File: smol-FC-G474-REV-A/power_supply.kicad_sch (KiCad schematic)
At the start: 0 parts

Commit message: Updated Buck-5V doc, added Buck 5V/10V and LDO for 3v3 on schematic
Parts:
- added C30, C35, C40, C42: 1u, symbol Device:C_Small
- added C31, C34: 4.7u, symbol Device:C_Small
- added C32, C33: 47u, symbol Device:C_Small
- added C36, C37, C38: 22u, symbol Device:C_Small
- added C39, C41: 10u, symbol Device:C_Small
- added L1: 1.5u, symbol Device:L
- added L2: 2.2u, symbol Device:L
- added R22, R25: 7.68K, symbol Device:R_Small
- added R26: 90.9K, symbol Device:R_Small
- added R27, R28, R29: 10K, symbol Device:R_Small
- added U10, U9: LP5912-3.3DRV, Package_SON:WSON-6-1EP_2x2mm_P0.65mm_EP1x1.6mm, symbol Regulator_Linear:LP5912-3.3DRV
- added U7, U8: LMQ66430R5RXBR, RXB0014A-MFG, symbol LMQ66430:PLMQ66430R5RXBR
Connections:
- new net +10V: C36.1, C37.1, C38.1, L2.2, R26.1
- new net +3V3_CORE: C40.1, R28.1, U9.1 (OUT)
- new net +3V3_SENS: C42.1, R29.1, U10.1 (OUT)
- new net +5V_BEC: C32.1, C33.1, L1.2, U7.11 (VOUT_FB)
- new net +5V_SYS: C39.1, C41.1, U10.4 (EN), U10.6 (IN), U9.4 (EN), U9.6 (IN)
- new net +VBAT: C31.1, C34.1, U7.1 (EN), U7.3 (VIN), U8.1 (EN), U8.3 (VIN)
- new net Buck-10V_FB: R26.2, R27.1, U8.11 (VOUT_FB)
- new net Buck-10V_RT: R25.1, U8.13 (RT)
- new net Buck-10V_SW: L2.1, U8.7 (SW)
- new net Buck-10V_VCC_INT: C35.1, U8.10 (VCC)
- new net Buck-5V_RT: R22.1, U7.13 (RT)
- new net Buck-5V_SW: L1.1, U7.7 (SW)
- new net Buck-5V_VCC_INT: C30.1, U7.10 (VCC)
- new net GND: C30.2, C31.2, C32.2, C33.2, C34.2, C35.2, C36.2, C37.2, C38.2, C39.2, C40.2, C41.2, C42.2, R22.2, R25.2, R27.2, U10.5 (GND), U10.7 (EP), U7.15 (GND_DAP), U7.6 (PGND), U8.15 (GND_DAP), U8.6 (PGND), U9.5 (GND), U9.7 (EP)
- new net LDO-C_PG: R28.2, U9.3 (PG)
- new net LDO-S_PG: R29.2, U10.3 (PG)
- no-connect marks 0 -> 4

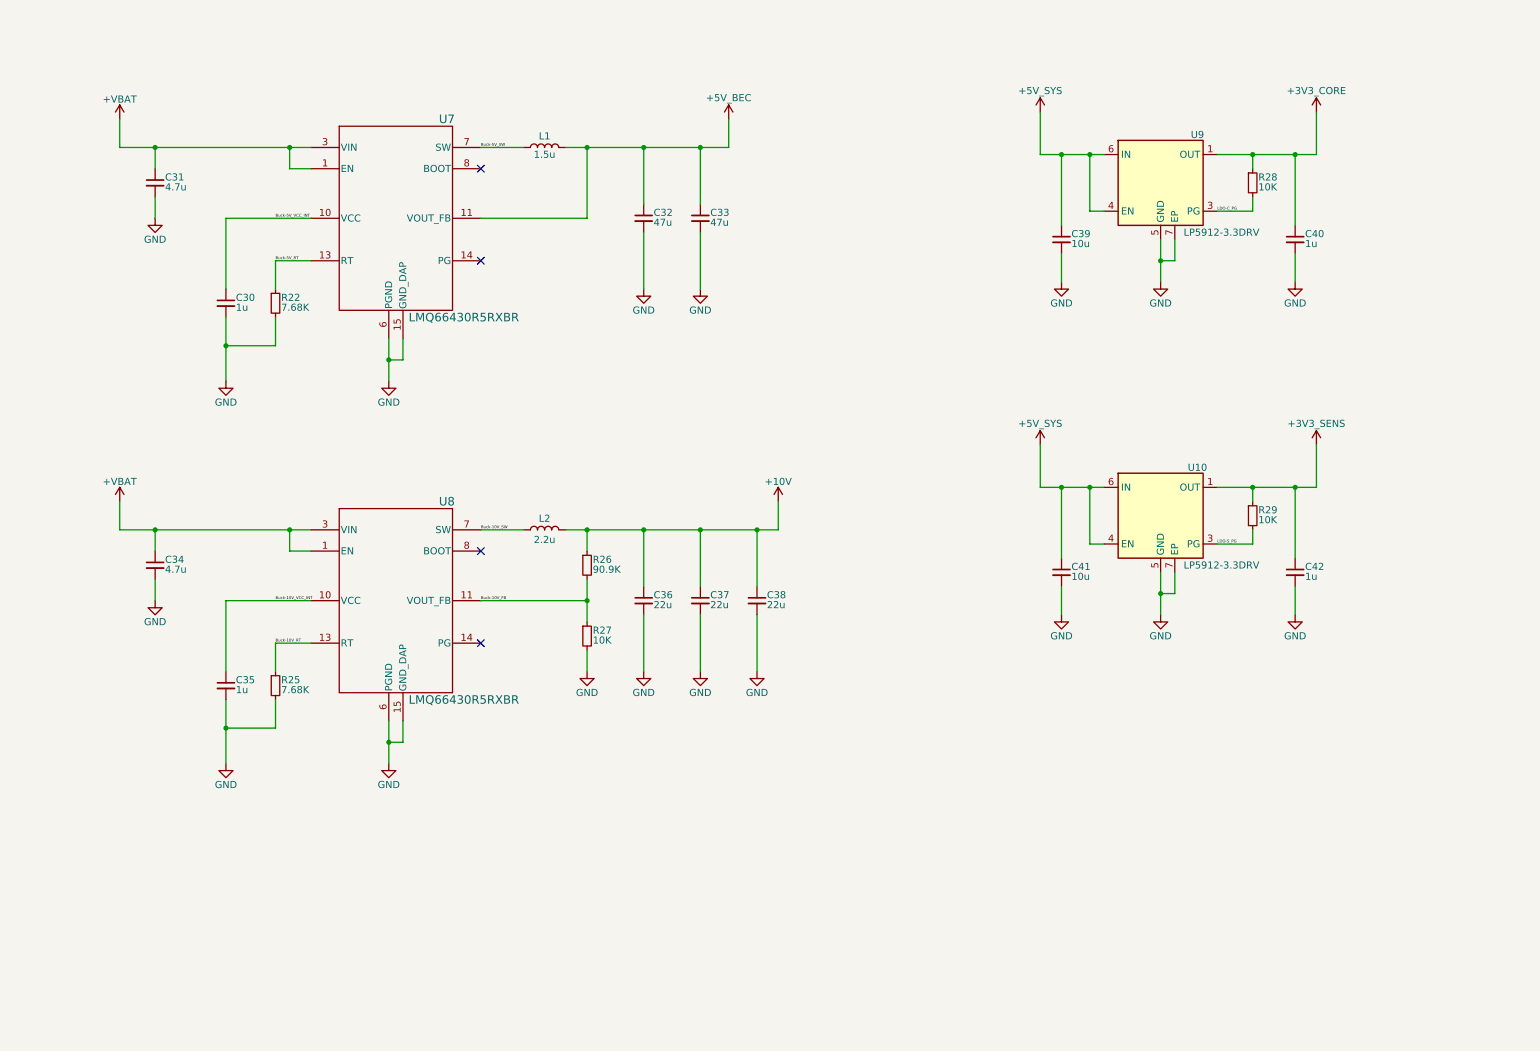
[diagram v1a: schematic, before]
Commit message: Changed 10V buck to 9V buck
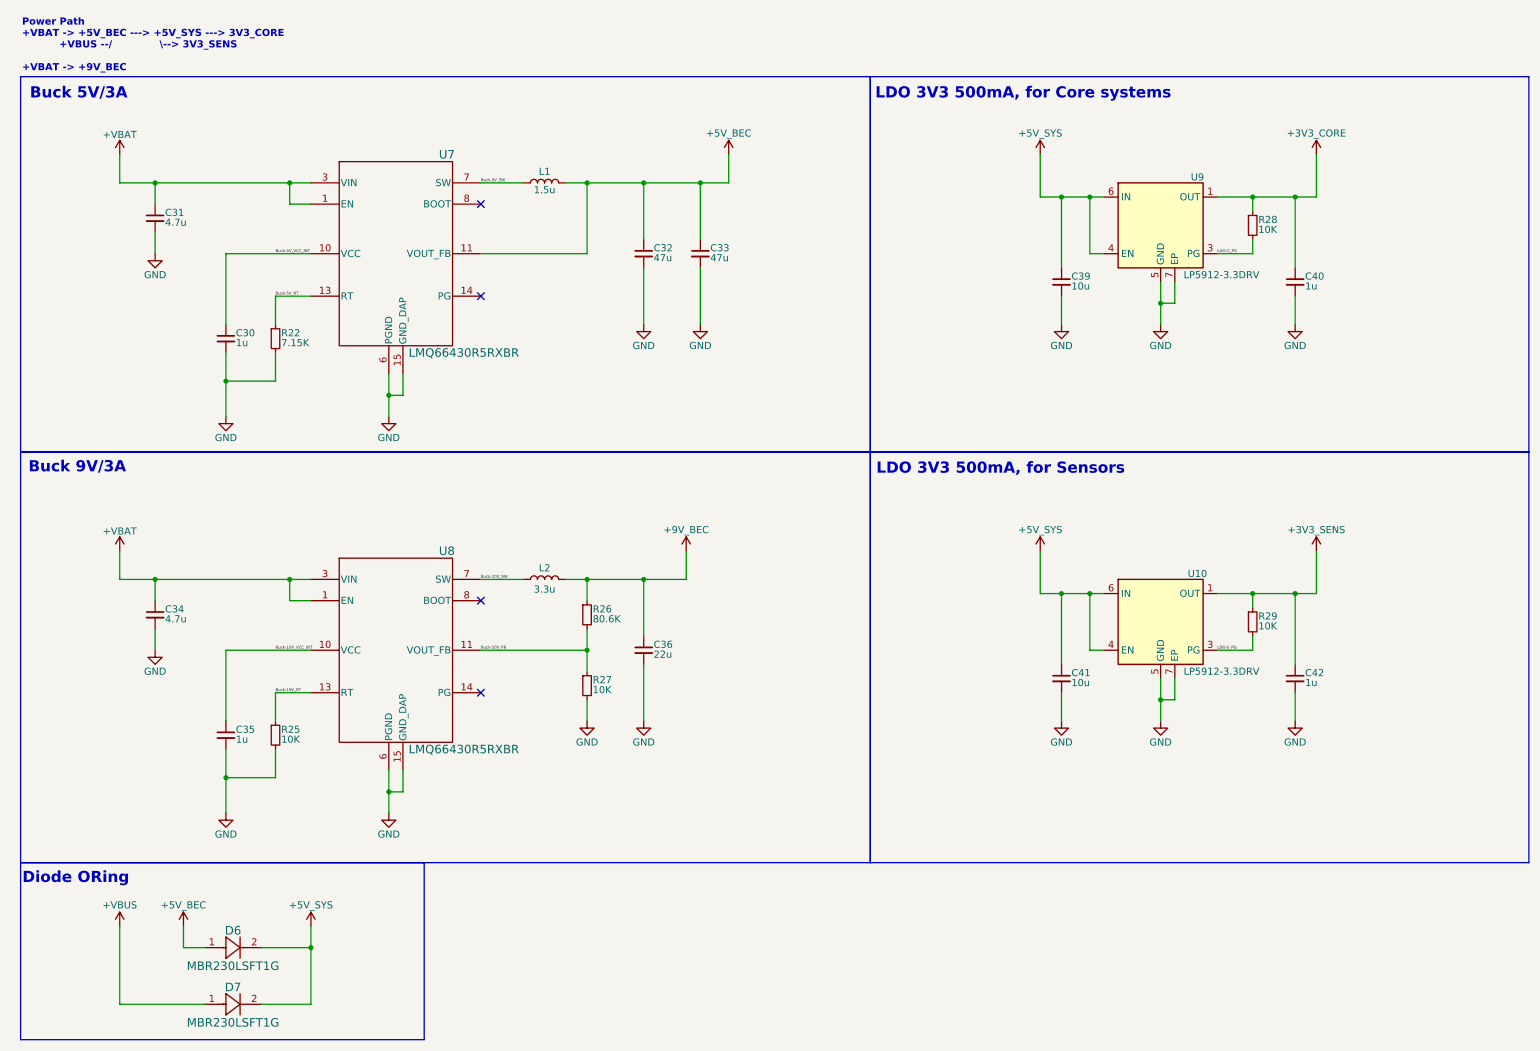
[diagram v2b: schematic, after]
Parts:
- removed C37, C38: 22u, symbol Device:C_Small
- added D6, D7: MBR230LSFT1G, symbol MBR230LSFT1G:MBR230LSFT1G
- L2: value 2.2u -> 3.3u
- R22: value 7.68K -> 7.15K
- R25: value 7.68K -> 10K
- R26: value 90.9K -> 80.6K
- U10, U9: footprint Package_SON:WSON-6-1EP_2x2mm_P0.65mm_EP1x1.6mm -> (none)
- U7, U8: footprint RXB0014A-MFG -> (none)
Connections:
- net +5V_BEC: now also D6.1
- net +5V_SYS: now also D6.2, D7.2
- net +10V renamed +9V_BEC
- new net +VBUS: D7.1
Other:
- note added: "Buck 5V/3A"
- note added: "Buck 9V/3A"
- note added: "Diode ORing"
- note added: "LDO 3V3 500mA, for Core systems"
- note added: "LDO 3V3 500mA, for Sensors"
- note added: "Power Path +VBAT -> +5V_BEC ---> +5V_SYS ---> 3V3_CORE +VBUS --/ \--> 3V3_SENS +VBAT -> +9V_BEC"
- moved on the sheet: C30, C31, C32, C33, C34, C35, C36, C39, C40, C41, C42, L1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

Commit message: Attached footprints and finalized schematic.
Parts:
- C30, C35: footprint (none) -> Capacitor_SMD:C_0603_1608Metric
- C31, C34: footprint (none) -> Capacitor_SMD:C_1206_3216Metric
- C32, C33, C36: footprint (none) -> Capacitor_SMD:C_0805_2012Metric
- C39, C40, C41, C42: footprint (none) -> Capacitor_SMD:C_0402_1005Metric
- D6, D7: footprint (none) -> MBR230LSFT1G:CR_0LSFT1G_ONS
- L1, L2: footprint (none) -> inductor-1.5u:AAPS0420M1R5F
- R22, R25, R26, R27, R28, R29: footprint (none) -> Resistor_SMD:R_0402_1005Metric
- U10, U9: footprint (none) -> Package_SON:WSON-6-1EP_2x2mm_P0.65mm_EP1x1.6mm
- U7, U8: footprint (none) -> LMQ66430:RXB0014A-MFG
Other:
- title: smol-FC-G474 -> smol-FC-G474-REV-A
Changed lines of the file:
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@@
 	(paper "A4")
 	(title_block
-		(title "smol-FC-G474")
-		(date "2026-05-31")
-		(rev "0.7.0")
+		(title "smol-FC-G474-REV-A")
+		(date "2026-06-05")
+		(rev "0.9.3")
 		(company "Daniel Plewa")
 		(comment 1 "License: CERN-OHL-W v2")
 		(comment 2 "GitHub: https://github.com/Def12345678/smol-FC-G474-REV-A")
-		(comment 3 "BEC 5A/2A, 10V/2A | Baro, OSD Chip and 16MB blackbox")
+		(comment 3 "BEC 5A/3A, 10V/3A | Baro, OSD Chip and 16MB blackbox")
 		(comment 4 "Open source flight controller on STM32G4, 20x20 3.5mm hole")
 	)
@@
 			)
 		)
-		(property "Footprint" ""
+		(property "Footprint" "inductor-1.5u:AAPS0420M1R5F"
 			(at 106.68 43.18 0)
 			(hide yes)
@@
 			)
 		)
-		(property "Footprint" ""
+		(property "Footprint" "Capacitor_SMD:C_0603_1608Metric"
 			(at 49.53 71.12 0)
 			(hide yes)
@@
 			)
 		)
-		(property "Footprint" ""
+		(property "Footprint" "Capacitor_SMD:C_0603_1608Metric"
 			(at 49.53 142.24 0)
 			(hide yes)
@@
 			)
 		)
-		(property "Footprint" ""
+		(property "Footprint" "Capacitor_SMD:C_1206_3216Metric"
 			(at 36.83 49.53 0)
 			(hide yes)
@@
 			)
 		)
-		(property "Footprint" ""
+		(property "Footprint" "Capacitor_SMD:C_0805_2012Metric"
 			(at 124.46 127 0)
 			(hide yes)
@@
 			)
 		)
-		(property "Footprint" ""
+		(property "Footprint" "Capacitor_SMD:C_0402_1005Metric"
 			(at 199.39 60.96 0)
 			(hide yes)
@@
 			)
 		)
-		(property "Footprint" ""
+		(property "Footprint" "Capacitor_SMD:C_0402_1005Metric"
 			(at 241.3 132.08 0)
 			(hide yes)
@@
 			)
 		)
-		(property "Footprint" ""
+		(property "Footprint" "Package_SON:WSON-6-1EP_2x2mm_P0.65mm_EP1x1.6mm"
 			(at 217.17 44.45 0)
 			(hide yes)
@@
 			)
 		)
-		(property "Footprint" ""
+		(property "Footprint" "Resistor_SMD:R_0402_1005Metric"
 			(at 114.3 133.35 0)
 			(hide yes)
@@
 			)
 		)
-		(property "Footprint" ""
+		(property "Footprint" "LMQ66430:RXB0014A-MFG"
 			(at 80.518 26.924 0)
 			(hide yes)
@@
 			)
 		)
-		(property "Footprint" ""
+		(property "Footprint" "MBR230LSFT1G:CR_0LSFT1G_ONS"
 			(at 55.88 190.5 0)
 			(hide yes)
@@
 			)
 		)
-		(property "Footprint" ""
+		(property "Footprint" "Capacitor_SMD:C_0402_1005Metric"
 			(at 199.39 132.08 0)
 			(hide yes)
@@
 			)
 		)
-		(property "Footprint" ""
+		(property "Footprint" "MBR230LSFT1G:CR_0LSFT1G_ONS"
 			(at 55.88 180.34 0)
 			(hide yes)
@@
 			)
 		)
-		(property "Footprint" ""
+		(property "Footprint" "Resistor_SMD:R_0402_1005Metric"
 			(at 58.42 71.12 0)
 			(hide yes)
@@
 			)
 		)
-		(property "Footprint" ""
+		(property "Footprint" "Package_SON:WSON-6-1EP_2x2mm_P0.65mm_EP1x1.6mm"
 			(at 217.17 115.57 0)
 			(hide yes)
@@
 			)
 		)
-		(property "Footprint" ""
+		(property "Footprint" "Capacitor_SMD:C_0805_2012Metric"
 			(at 134.62 55.88 0)
 			(hide yes)
@@
 			)
 		)
-		(property "Footprint" ""
+		(property "Footprint" "Capacitor_SMD:C_0805_2012Metric"
 			(at 124.46 55.88 0)
 			(hide yes)
@@
 			)
 		)
-		(property "Footprint" ""
+		(property "Footprint" "Capacitor_SMD:C_1206_3216Metric"
 			(at 36.83 120.65 0)
 			(hide yes)
@@
 			)
 		)
-		(property "Footprint" ""
+		(property "Footprint" "Capacitor_SMD:C_0402_1005Metric"
 			(at 241.3 60.96 0)
 			(hide yes)
@@
 			)
 		)
-		(property "Footprint" ""
+		(property "Footprint" "Resistor_SMD:R_0402_1005Metric"
 			(at 114.3 120.65 0)
 			(hide yes)
@@
 			)
 		)
-		(property "Footprint" ""
+		(property "Footprint" "Resistor_SMD:R_0402_1005Metric"
 			(at 233.68 50.8 0)
 			(hide yes)
@@
 			)
 		)
-		(property "Footprint" ""
+		(property "Footprint" "inductor-1.5u:AAPS0420M1R5F"
 			(at 106.68 114.3 0)
 			(hide yes)
@@
 			)
 		)
-		(property "Footprint" ""
+		(property "Footprint" "LMQ66430:RXB0014A-MFG"
 			(at 80.518 98.044 0)
 			(hide yes)
@@
 			)
 		)
-		(property "Footprint" ""
+		(property "Footprint" "Resistor_SMD:R_0402_1005Metric"
 			(at 58.42 142.24 0)
 			(hide yes)
@@
 			)
 		)
-		(property "Footprint" ""
+		(property "Footprint" "Resistor_SMD:R_0402_1005Metric"
 			(at 233.68 121.92 0)
 			(hide yes)

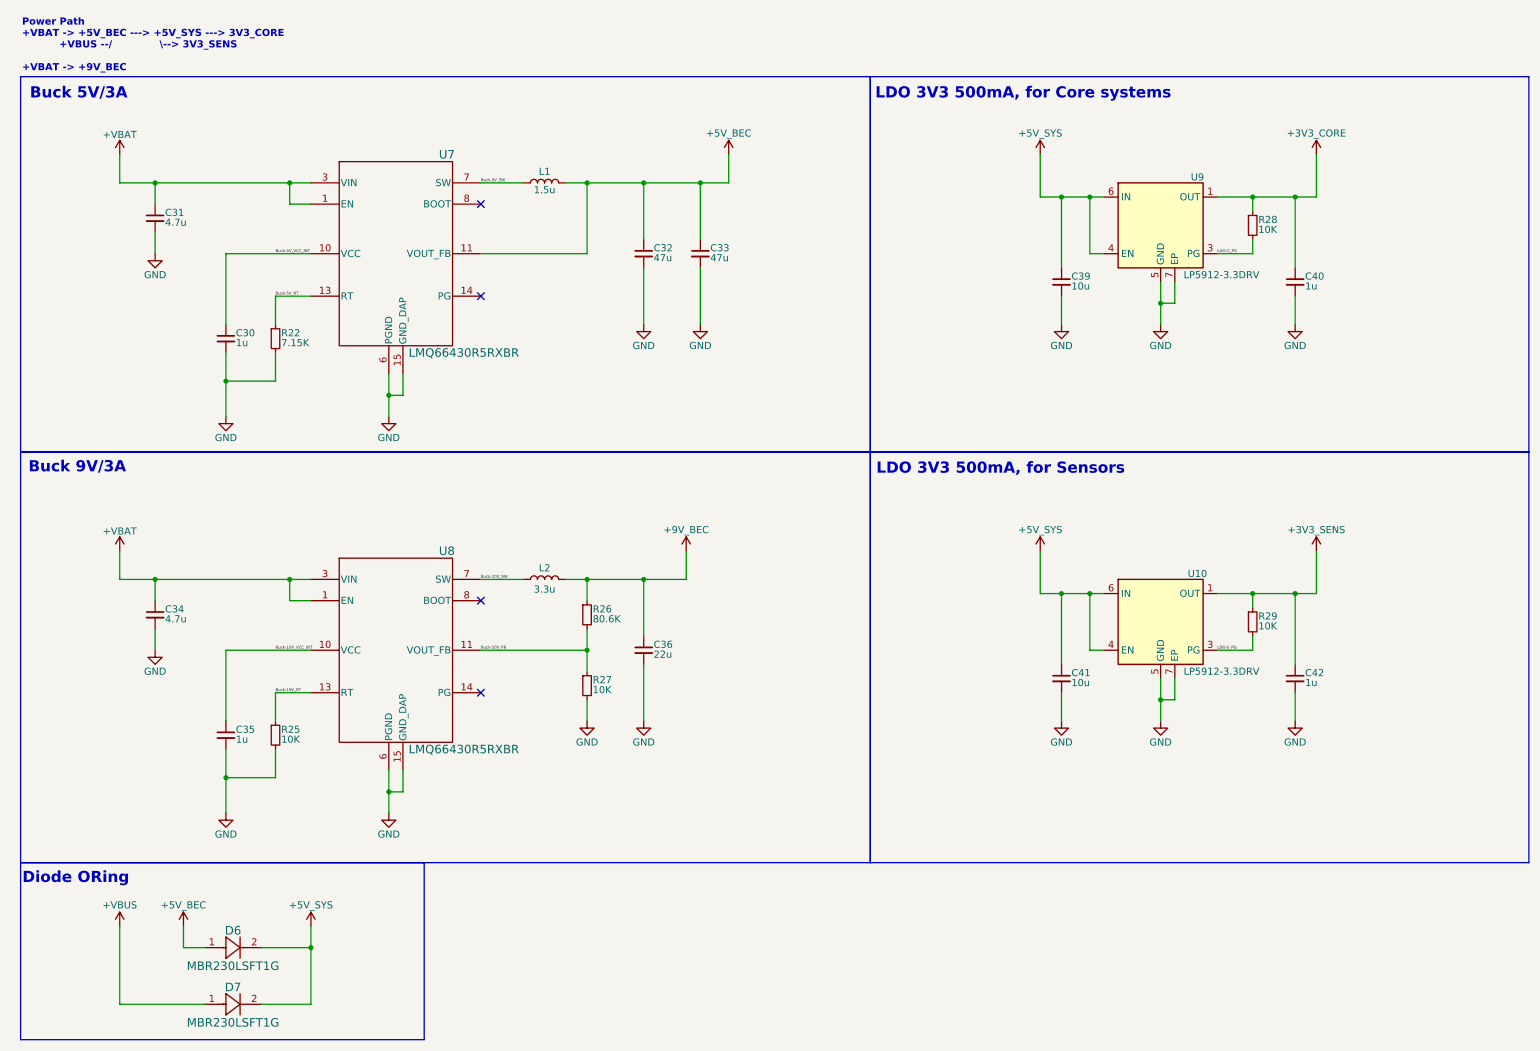
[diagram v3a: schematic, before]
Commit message: Finalized schematic, added power mux
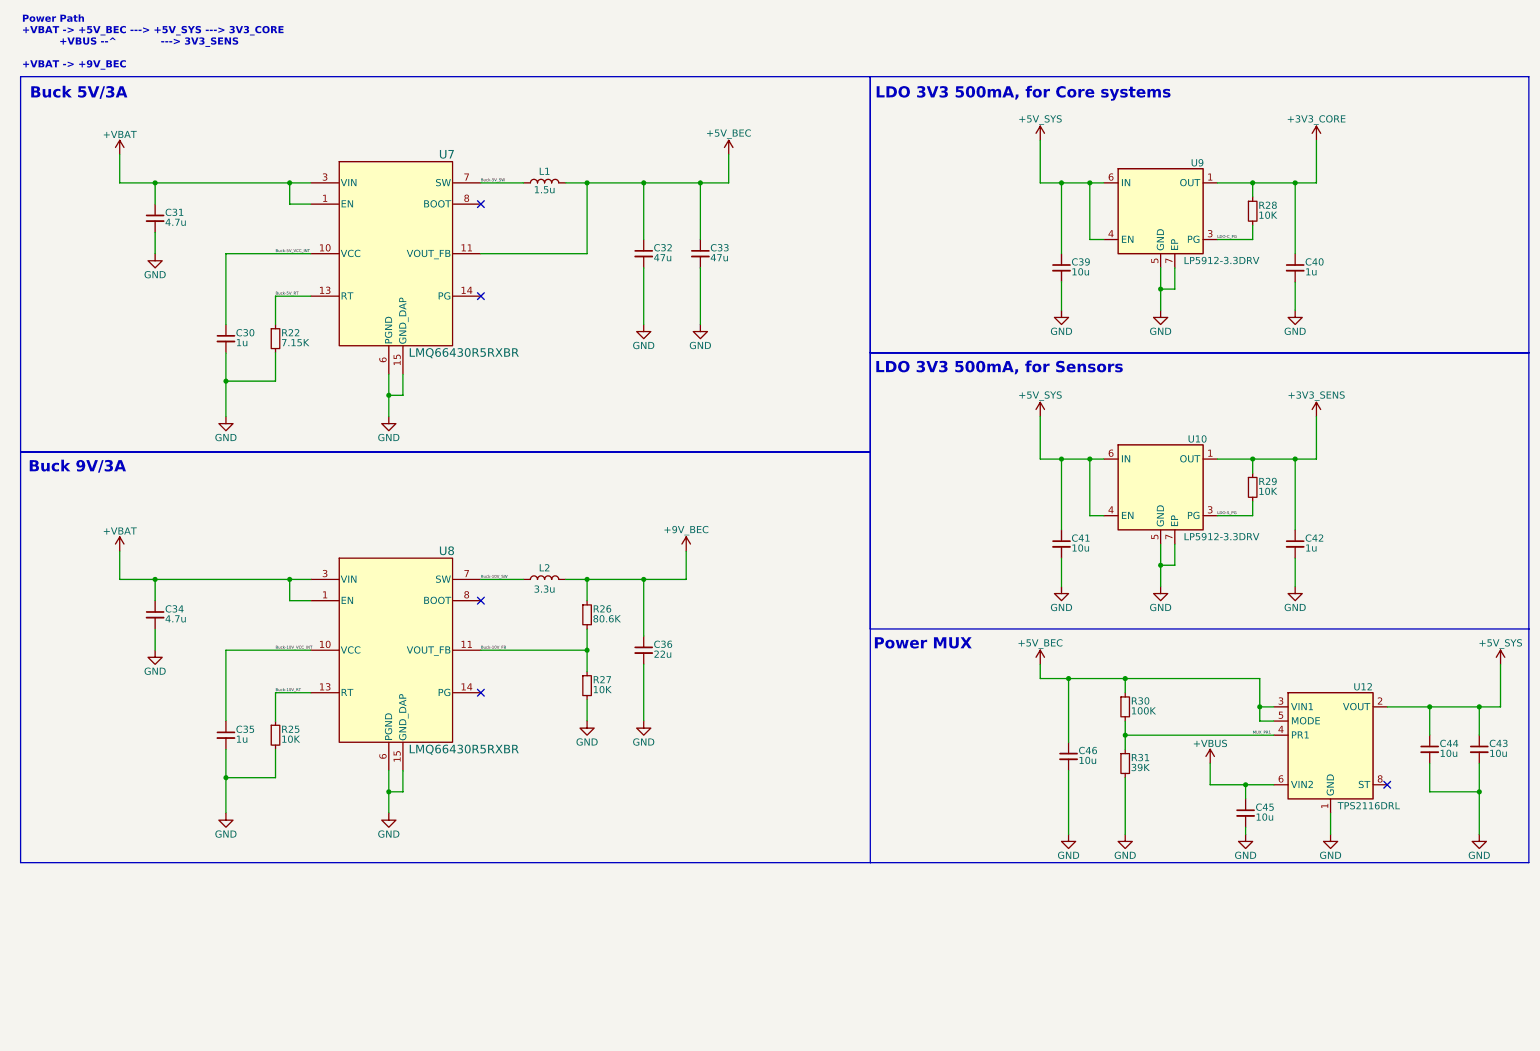
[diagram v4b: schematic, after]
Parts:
- removed D6, D7: MBR230LSFT1G, MBR230LSFT1G:CR_0LSFT1G_ONS, symbol MBR230LSFT1G:MBR230LSFT1G
- added C43, C44, C45, C46: 10u, Capacitor_SMD:C_0402_1005Metric, symbol Device:C_Small
- added R30: 100K, Resistor_SMD:R_0402_1005Metric, symbol Device:R_Small
- added R31: 39K, Resistor_SMD:R_0402_1005Metric, symbol Device:R_Small
- added U12: TPS2116DRL, Package_TO_SOT_SMD:SOT-583-8, symbol Power_Management:TPS2116DRL
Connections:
- net +5V_BEC: now also C46.1, R30.1, U12.3 (VIN1), U12.5 (MODE)
- net +5V_SYS: now also C43.1, C44.1, U12.2 (VOUT), U12.7 (VOUT)
- net +VBUS: now also C45.1, U12.6 (VIN2)
- net GND: now also C43.2, C44.2, C45.2, C46.2, R31.2, U12.1 (GND)
- new net MUX_PR1: R30.2, R31.1, U12.4 (PR1)
- no-connect marks 4 -> 5
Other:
- note added: "Power MUX"
- note added: "Power Path +VBAT -> +5V_BEC ---> +5V_SYS ---> 3V3_CORE +VBUS --^ ---> 3V3_SENS +VBAT -> +9V_BEC"
- note removed: "Diode ORing"
- note removed: "Power Path +VBAT -> +5V_BEC ---> +5V_SYS ---> 3V3_CORE +VBUS --/ \--> 3V3_SENS +VBAT -> +9V_BEC"
- moved on the sheet: C39, C40, C41, C42, R28, R29, U10, U9

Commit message: In progress PCB layout
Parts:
- C29: renamed from C31; footprint Capacitor_SMD:C_1206_3216Metric -> Capacitor_SMD:C_0805_2012Metric
- C37: renamed from C34; footprint Capacitor_SMD:C_1206_3216Metric -> Capacitor_SMD:C_0805_2012Metric
- L1: footprint inductor-1.5u:AAPS0420M1R5F -> inductor:IND-SMD_L3.0-W3.0_YSMC0320H
- L2: footprint inductor-1.5u:AAPS0420M1R5F -> inductor:APH0430C-3R3M-TCD5
- R20: renamed from R28; value 10K -> 10k
- R21: renamed from R22; value 7.15K -> 7.15k
- R22: renamed from R29; value 10K -> 10k
- R23: renamed from R26; value 80.6K -> 80.6k
- R24: renamed from R27; value 10K -> 10k
- R25: renamed from R30; value 100K -> 100k
- R26: renamed from R25; value 10K -> 10k
- R27: renamed from R31; value 39K -> 39k
- renumbered C32 to C30, C33 to C31, C39 to C32, C40 to C33, C30 to C34, C41 to C35, C42 to C36, C36 to C38, C35 to C39, C44 to C40, C43 to C41, C46 to C42, C45 to C43, U8 to U11, U7 to U8
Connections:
- net Buck-10V_FB renamed Buck-9V_FB
- net Buck-10V_RT renamed Buck-9V_RT
- net Buck-10V_SW renamed Buck-9V_SW
- net Buck-10V_VCC_INT renamed Buck-9V_VCC_INT
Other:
- note added: "Buck 5V/2A"
- note removed: "Buck 5V/3A"
